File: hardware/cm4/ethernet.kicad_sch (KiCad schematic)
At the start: 5 parts, among them J14 HR911105A, U12 TPD4EUSB30

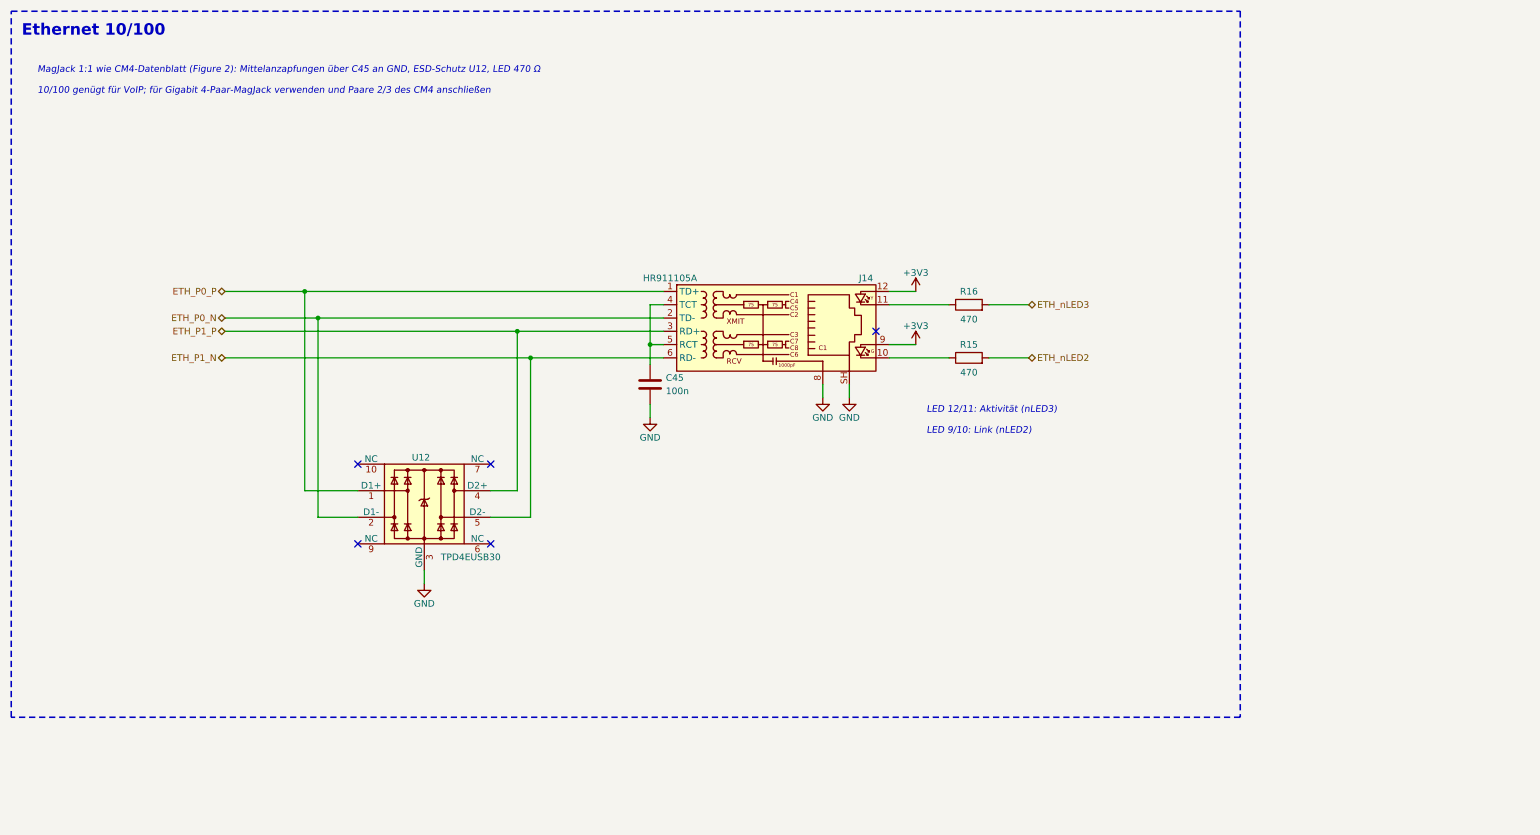
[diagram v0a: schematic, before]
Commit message: CM4-Schaltplan: Einzelblock-Blätter ohne Rahmen, Inhalt zentriert
kicadgen: Steht nur ein Block auf einem Blatt, entfällt der Rahmen (sein Titel wird
Blatttitel) und der Inhalt wird auf dem Blatt zentriert (über dem Schriftfeld, auf dem
1,27-mm-Raster). Hinweistexte der CM4-Blätter an die Schaltungen gerückt.

Co-Authored-By: Claude Opus 5.5 <noreply@anthropic.com>
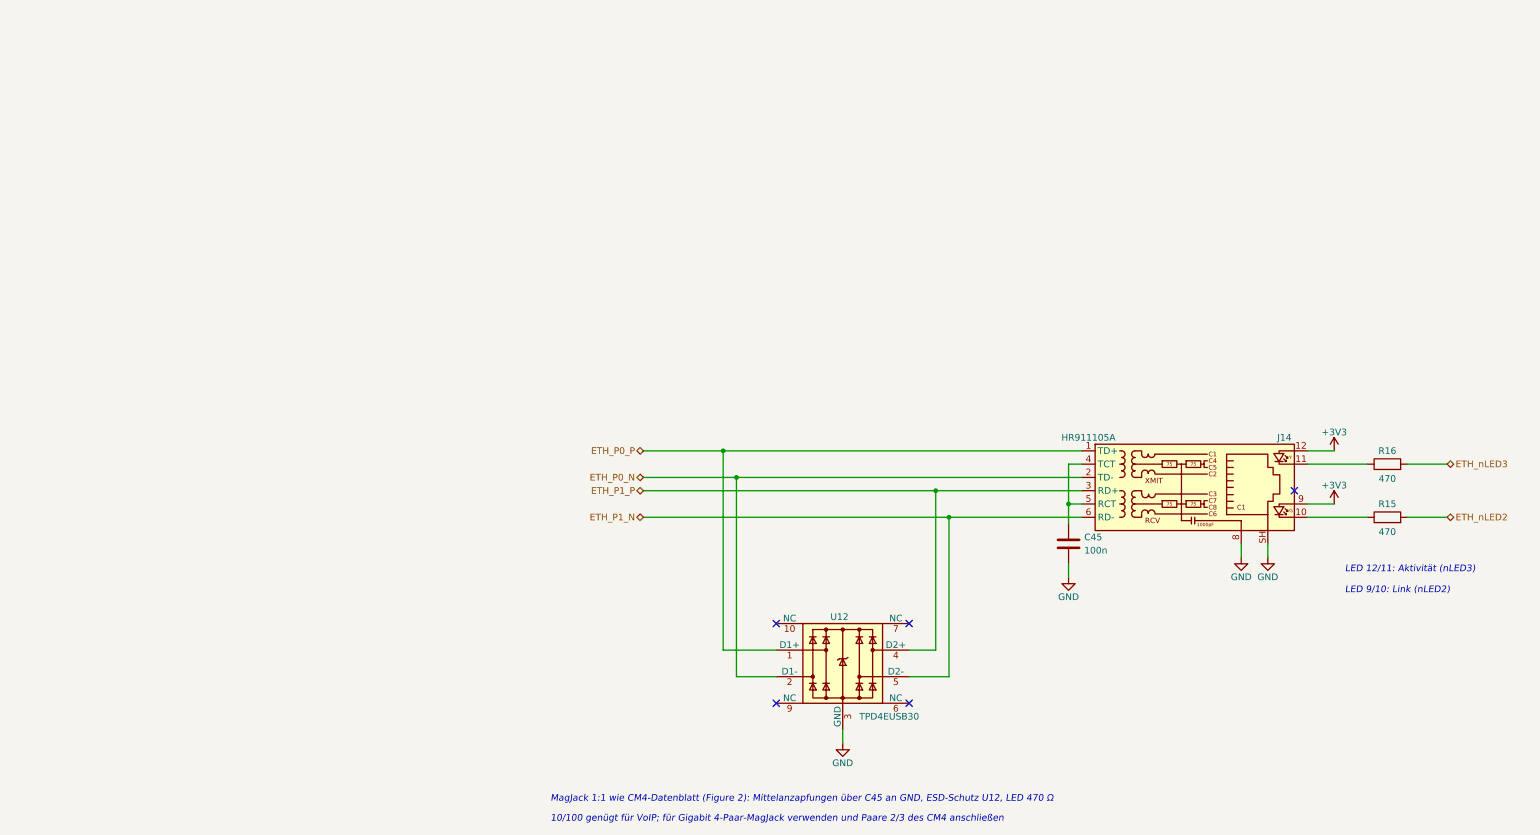
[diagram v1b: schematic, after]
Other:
- note removed: "Ethernet 10/100"
- title: Ethernet -> Ethernet 10/100
